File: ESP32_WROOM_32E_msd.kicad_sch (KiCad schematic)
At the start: 1 part, among them U1 ESP32-WROOM-32E

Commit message: complete pcb
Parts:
- removed U1: ESP32-WROOM-32E, RF_Module:ESP32-WROOM-32D, symbol RF_Module:ESP32-WROOM-32E
- added C1: 4700, Capacitor_SMD:C_0603_1608Metric, symbol Device:C
- added D1, D2: LED, LED_SMD:LED_0603_1608Metric, symbol Device:LED
- added H1, H2, H3, H4: MountingHole_Pad, MountingHole:MountingHole_3.2mm_M3_DIN965_Pad, symbol Mechanical:MountingHole_Pad
- added J1, J2: XH_6pin, Connector_JST:JST_XH_B6B-XH-A_1x06_P2.50mm_Vertical, symbol Connector:Conn_01x06_Socket
- added J3, J4: XH_2pin, Connector_JST:JST_XH_B2B-XH-A_1x02_P2.50mm_Vertical, symbol Connector:Conn_01x02_Socket
- added R1: 300, Resistor_SMD:R_0603_1608Metric, symbol Device:R
- added R2, R3: 60, Resistor_SMD:R_0603_1608Metric, symbol Device:R
- added R4: 120, Resistor_SMD:R_0603_1608Metric, symbol Device:R
- added R5, R6: 1k, Resistor_SMD:R_0603_1608Metric, symbol Device:R
- added SW1: SW_SPDT, Original:slide_SW, symbol Switch:SW_SPDT
- added U1: ~, my_library:MODULE_ESP32-DEVKITC-32E, symbol ESP32-DEVKITC-32E:ESP32-DEVKITC-32E
- added U2: MCP2561-E-SN, Package_SO:SOIC-8_3.9x4.9mm_P1.27mm, symbol Interface_CAN_LIN:MCP2561-E-SN
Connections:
- new net: C1.1, R1.2, R2.2, R3.1
- new net: D2.2 (A), R6.2
- new net: R1.1, U2.5 (SPLIT)
- new net: R4.1, SW1.1 (A)
- new net: D1.2 (A), R5.2
- new net +5V: U1.J2_19 (EXT_5V), U2.3 (VDD)
- new net CAN_H: J3.1 (Pin_1), R2.1, SW1.2 (B), U2.7 (CANH)
- new net CAN_L: J3.2 (Pin_2), R3.2, R4.2, U2.6 (CANL)
- new net CAN_RXD: U1.J2_10 (IO26), U2.4 (RXD)
- new net CAN_TXD: U1.J2_11 (IO27), U2.1 (TXD)
- new net GND: C1.2, D1.1 (K), D2.1 (K), H1.1, H2.1, H3.1, H4.1, U1.J3_1 (GND_J3_1), U2.2 (VSS), U2.8 (STBY)
- new net LB_1: J2.5 (Pin_5), U1.J2_9 (IO25)
- new net LB_2: J2.4 (Pin_4), U1.J2_12 (IO14)
- new net LB_PWM: J2.6 (Pin_6), U1.J2_15 (IO13)
- new net LD1: R5.1, U1.J3_15 (IO2)
- new net LD2: R6.1, U1.J3_16 (IO15)
- new net LF_1: J1.5 (Pin_5), U1.J3_9 (IO18)
- new net LF_2: J1.4 (Pin_4), U1.J3_8 (IO19)
- new net LF_PWM: J1.6 (Pin_6), U1.J3_6 (IO21)
- new net RB_1: J2.3 (Pin_3), U1.J2_7 (IO32)
- new net RB_2: J2.2 (Pin_2), U1.J2_8 (IO33)
- new net RB_PWM: J2.1 (Pin_1), U1.J3_13 (IO4)
- new net RF_1: J1.3 (Pin_3), U1.J3_3 (IO22)
- new net RF_2: J1.2 (Pin_2), U1.J3_2 (IO23)
- new net RF_PWM: J1.1 (Pin_1), U1.J3_12 (IO16)
- new net UART_RX: J4.2 (Pin_2), U1.J3_5 (RXD0)
- new net UART_TX: J4.1 (Pin_1), U1.J3_4 (TXD0)
- no-connect marks 0 -> 19
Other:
- note added: "ESP32-WROOM32E-Devkitc"
- company: (none) -> RyutaroMasuda

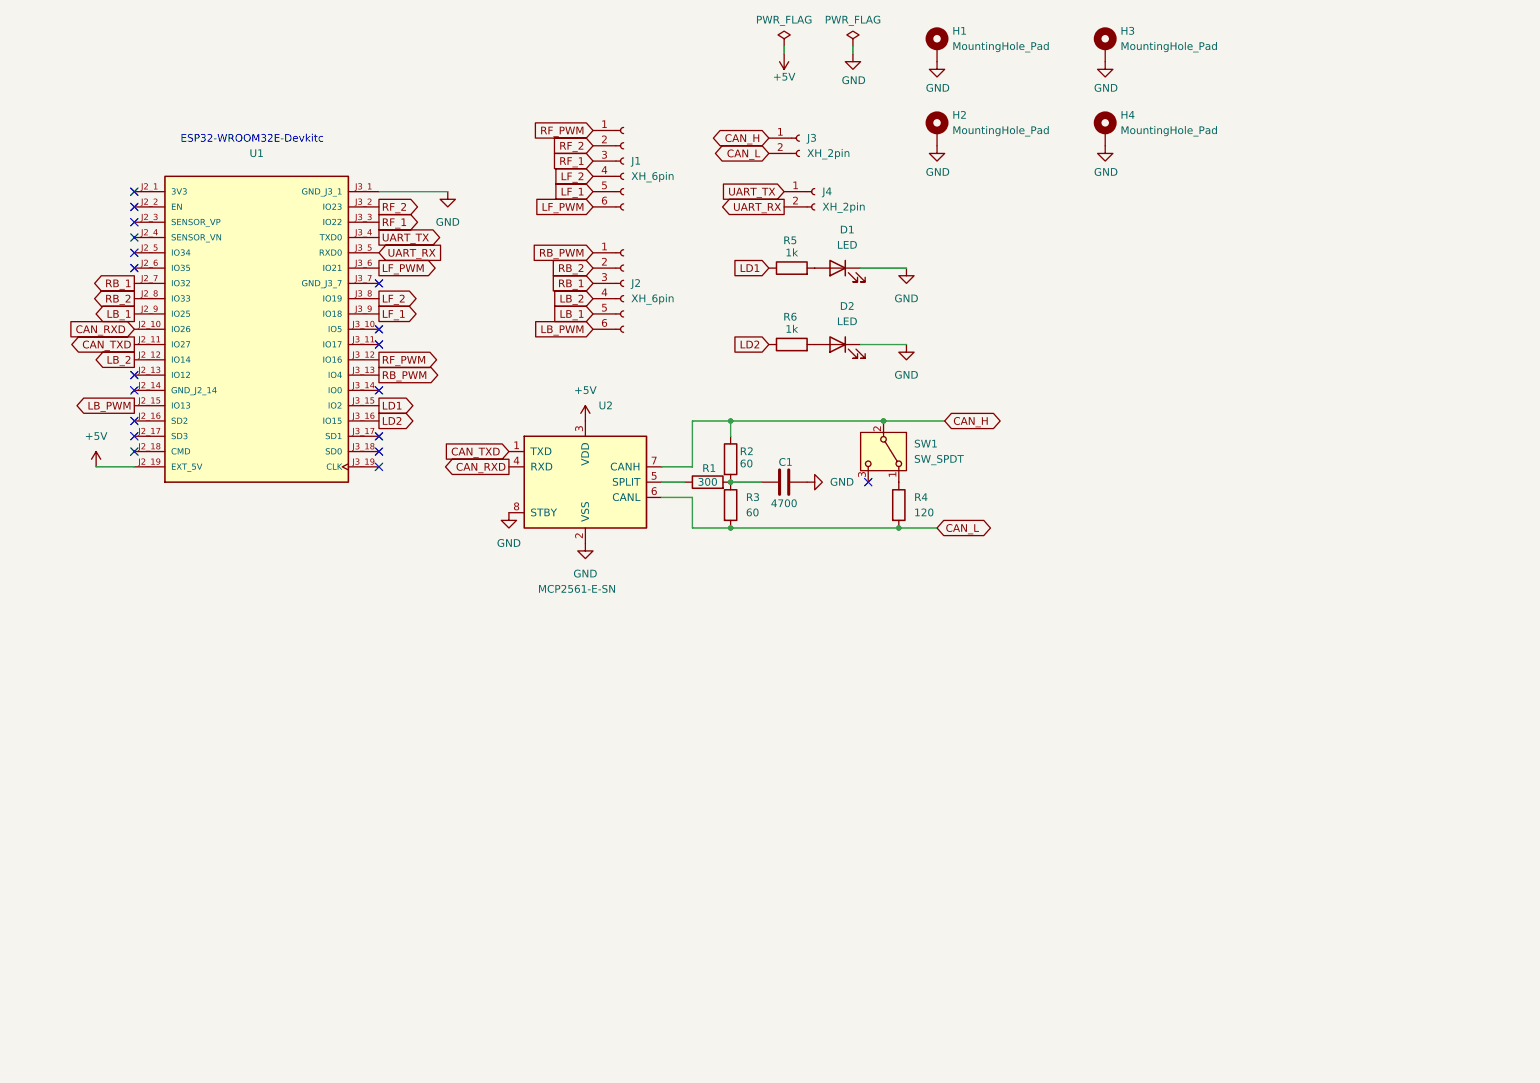
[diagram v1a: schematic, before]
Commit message: add encoder pin and motor driver pin
XH_4×4, pin header_8×1
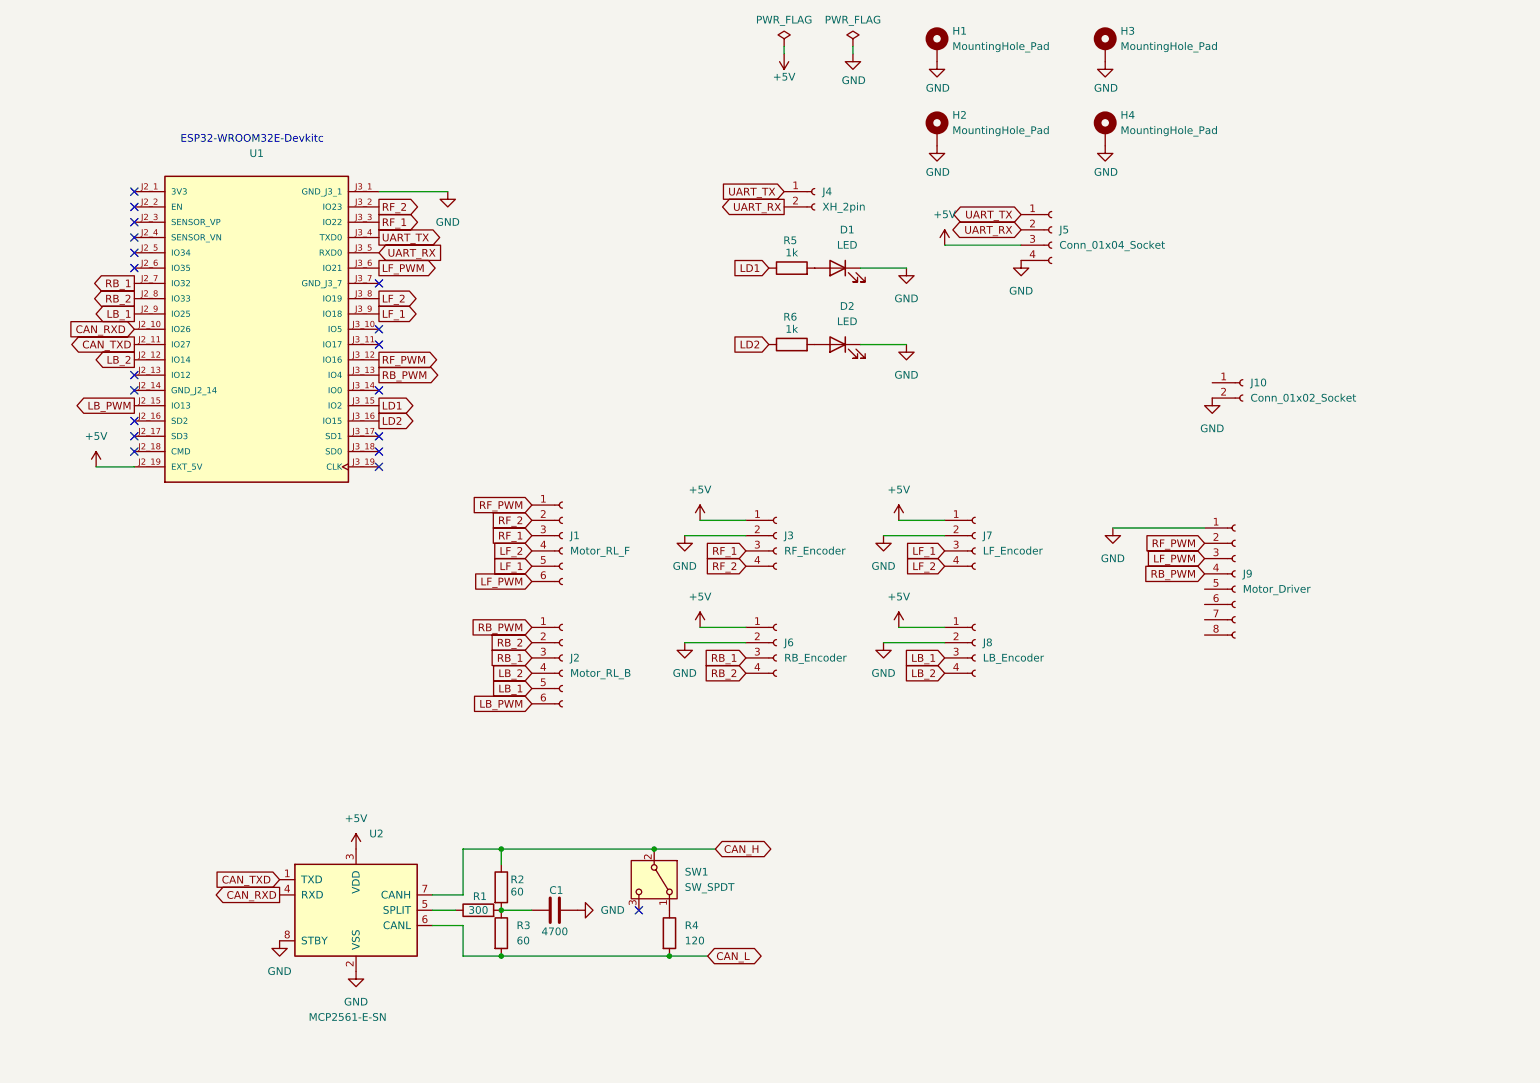
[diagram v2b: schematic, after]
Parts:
- removed J3: XH_2pin, Connector_JST:JST_XH_B2B-XH-A_1x02_P2.50mm_Vertical, symbol Connector:Conn_01x02_Socket
- added J10: Conn_01x02_Socket, symbol Connector:Conn_01x02_Socket
- added J3: RF_Encoder, symbol Connector:Conn_01x04_Socket
- added J5: Conn_01x04_Socket, Connector_JST:JST_XH_B4B-XH-A_1x04_P2.50mm_Vertical, symbol Connector:Conn_01x04_Socket
- added J6: RB_Encoder, symbol Connector:Conn_01x04_Socket
- added J7: LF_Encoder, symbol Connector:Conn_01x04_Socket
- added J8: LB_Encoder, symbol Connector:Conn_01x04_Socket
- added J9: Motor_Driver, symbol Connector:Conn_01x08_Socket
- J1: value XH_6pin -> Motor_RL_F
- J2: value XH_6pin -> Motor_RL_B
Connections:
- net +5V: now also J3.1 (Pin_1), J5.3 (Pin_3), J6.1 (Pin_1), J7.1 (Pin_1), J8.1 (Pin_1)
- net GND: now also J10.2 (Pin_2), J3.2 (Pin_2), J5.4 (Pin_4), J6.2 (Pin_2), J7.2 (Pin_2), J8.2 (Pin_2), J9.1 (Pin_1)
- net LB_1: now also J8.3 (Pin_3)
- net LB_2: now also J8.4 (Pin_4)
- net LF_1: now also J7.3 (Pin_3)
- net LF_2: now also J7.4 (Pin_4)
- net LF_PWM: now also J9.3 (Pin_3)
- net RB_1: now also J6.3 (Pin_3)
- net RB_2: now also J6.4 (Pin_4)
- net RB_PWM: now also J9.4 (Pin_4)
- net RF_1: now also J3.3 (Pin_3)
- net RF_2: now also J3.4 (Pin_4)
- net RF_PWM: now also J9.2 (Pin_2)
- net UART_RX: now also J5.2 (Pin_2)
- net UART_TX: now also J5.1 (Pin_1)
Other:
- moved on the sheet: C1, J1, J2, R1, R2, R3, R4, SW1, U2

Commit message: add frames
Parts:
- removed J4: XH_2pin, Connector_JST:JST_XH_B2B-XH-A_1x02_P2.50mm_Vertical, symbol Connector:Conn_01x02_Socket
- removed R4: 120, Resistor_SMD:R_0603_1608Metric, symbol Device:R
- added J11, J12: Conn_01x03_Socket, symbol Connector:Conn_01x03_Socket
- J10: value Conn_01x02_Socket -> 7.5V
- J3, J6, J7, J8: footprint (none) -> Connector_JST:JST_XH_B4B-XH-A_1x04_P2.50mm_Vertical
- J5: value Conn_01x04_Socket -> CAN_External_Pin
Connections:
- net CAN_H: no longer R2.1
- net GND: now also J11.3 (Pin_3), J12.3 (Pin_3)
- net LB_PWM: now also J11.1 (Pin_1)
- net at SW1.1 (A): now also R2.1
- net +7.5V: now reaches J10.1 (Pin_1)
- net +7.5V: now also J9.5 (Pin_5), J11.2 (Pin_2), J12.2 (Pin_2)
- net Servo1: now reaches U1.J3_10 (IO5)
- net Servo1: now also J12.1 (Pin_1)
- net MOTOR_OUT1: now reaches J9.6 (Pin_6)
- net MOTOR_OUT2: now reaches J9.8 (Pin_8)
- net UART_RX: no longer names the net of U1.J3_5 (RXD0)
- net UART_RX: no longer J5.2 (Pin_2)
- net UART_TX: no longer names the net of U1.J3_4 (TXD0)
- net UART_TX: no longer J5.1 (Pin_1)
- new net CAN_RX: J5.2 (Pin_2)
- new net CAN_TX: J5.1 (Pin_1)
- no-connect marks 19 -> 21
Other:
- note added: "CAN_Communication"
- note added: "Mechanam_Encoder"
- note added: "Mechanam_Motor_Driver"
- note added: "Other_Actuator"
- moved on the sheet: C1, D1, D2, H1, H2, H3, H4, J1, J10, J2, J3, J5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

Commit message: almost complete
add Beta Ground,
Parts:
- added DC_motor1: DC_Motor, Connector_JST:JST_XH_B2B-XH-A_1x02_P2.50mm_Vertical, symbol Connector:Conn_01x02_Socket
- J10: footprint (none) -> Connector_AMASS:AMASS_XT30PW-F_1x02_P2.50mm_Horizontal
- J9: footprint (none) -> Connector_PinHeader_2.54mm:PinHeader_1x08_P2.54mm_Vertical
- Servo_1: renamed from J12; value Conn_01x03_Socket -> Servo_1; footprint (none) -> Connector_JST:JST_XH_B3B-XH-A_1x03_P2.50mm_Vertical
- Servo_2: renamed from J11; value Conn_01x03_Socket -> Servo_2; footprint (none) -> Connector_JST:JST_XH_B3B-XH-A_1x03_P2.50mm_Vertical
- renumbered J5 to CAN1, J8 to LB_Encoder1, J7 to LF_Encoder1, J2 to Motor_RL_B1, J1 to Motor_RL_F1, J6 to RB_Encoder1, J3 to RF_Encoder1
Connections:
- net CAN_RX is gone; now on net CAN_L: CAN1.2 (Pin_2)
- net CAN_TX is gone; now on net CAN_H: CAN1.1 (Pin_1)
- net +7.5V: now also J10.2 (Pin_2); no longer J10.1 (Pin_1)
- net GND: now also J10.1 (Pin_1); no longer J10.2 (Pin_2)
- net LB_1: now also LB_Encoder1.4 (Pin_4); no longer LB_Encoder1.3 (Pin_3)
- net LB_2: now also LB_Encoder1.3 (Pin_3); no longer LB_Encoder1.4 (Pin_4)
- net LF_1: now also LF_Encoder1.4 (Pin_4); no longer LF_Encoder1.3 (Pin_3)
- net LF_2: now also LF_Encoder1.3 (Pin_3); no longer LF_Encoder1.4 (Pin_4)
- net MOTOR_OUT1: now also DC_motor1.1 (Pin_1)
- net MOTOR_OUT2: now also DC_motor1.2 (Pin_2)
- net RB_1: now also RB_Encoder1.4 (Pin_4); no longer RB_Encoder1.3 (Pin_3)
- net RB_2: now also RB_Encoder1.3 (Pin_3); no longer RB_Encoder1.4 (Pin_4)
- net RF_1: now also RF_Encoder1.4 (Pin_4); no longer RF_Encoder1.3 (Pin_3)
- net RF_2: now also RF_Encoder1.3 (Pin_3); no longer RF_Encoder1.4 (Pin_4)
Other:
- moved on the sheet: J9
